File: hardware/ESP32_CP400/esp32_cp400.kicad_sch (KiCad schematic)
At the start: 20 parts, among them J2 USB_A, J3 USB_A, J4 USB_A, J5 Micro_SD_Card, J6 Barrel_Jack, J7 DA15_Pins

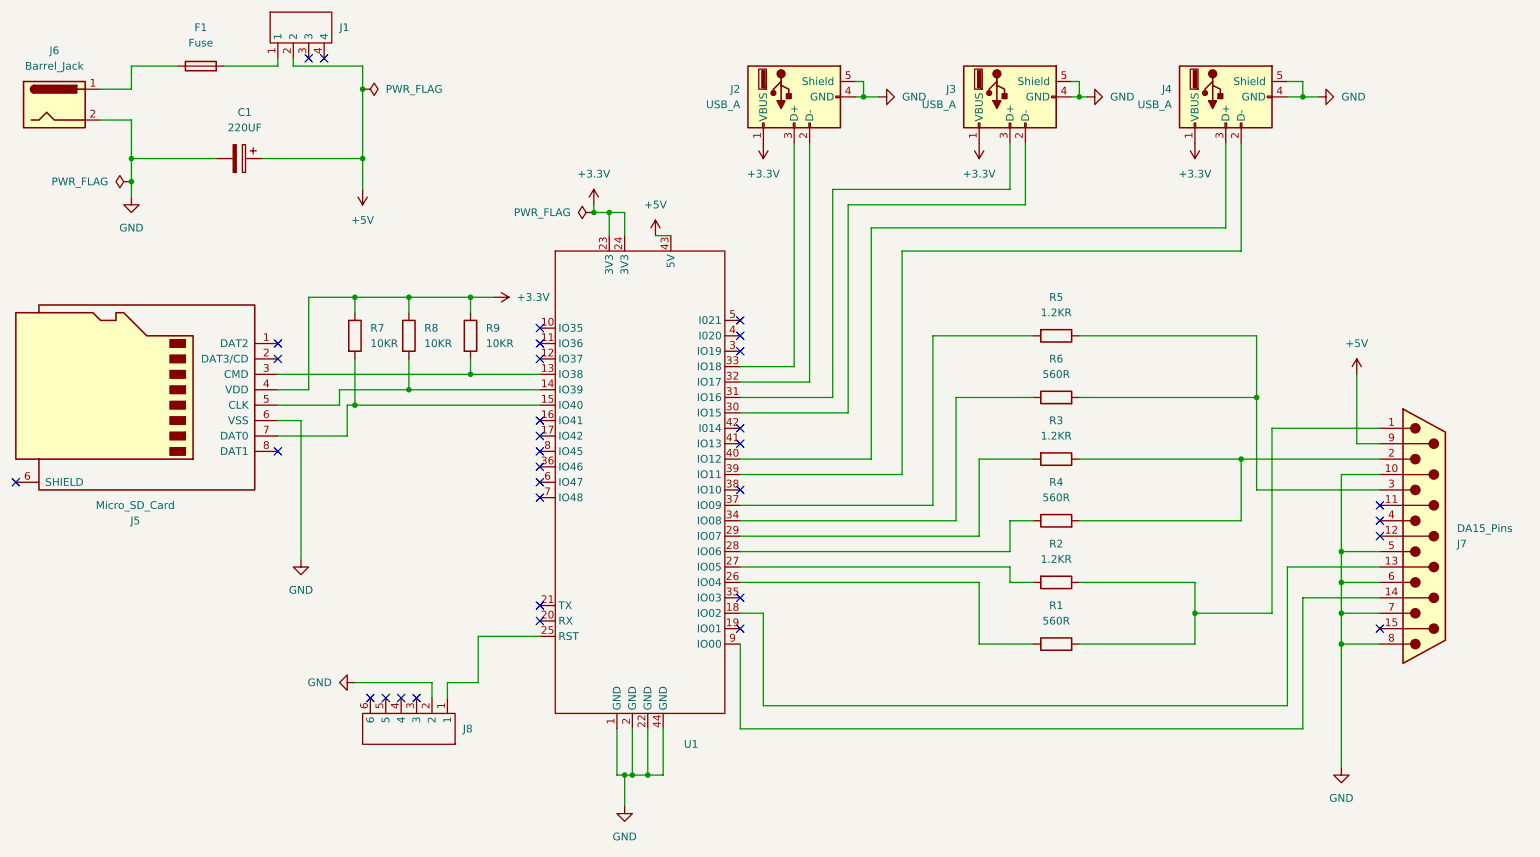
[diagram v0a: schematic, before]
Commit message: Add footprint for PJ-307 connector
- Created a new footprint file for the PJ-307 connector in the KiCad format.
- Included necessary attributes such as reference, value, and layer specifications.
- Defined pads for through-hole connections with appropriate sizes and drill specifications.
- Added graphical elements including lines and polygons for silk screen and fabrication layers.
- Provided a link to the datasheet for reference.
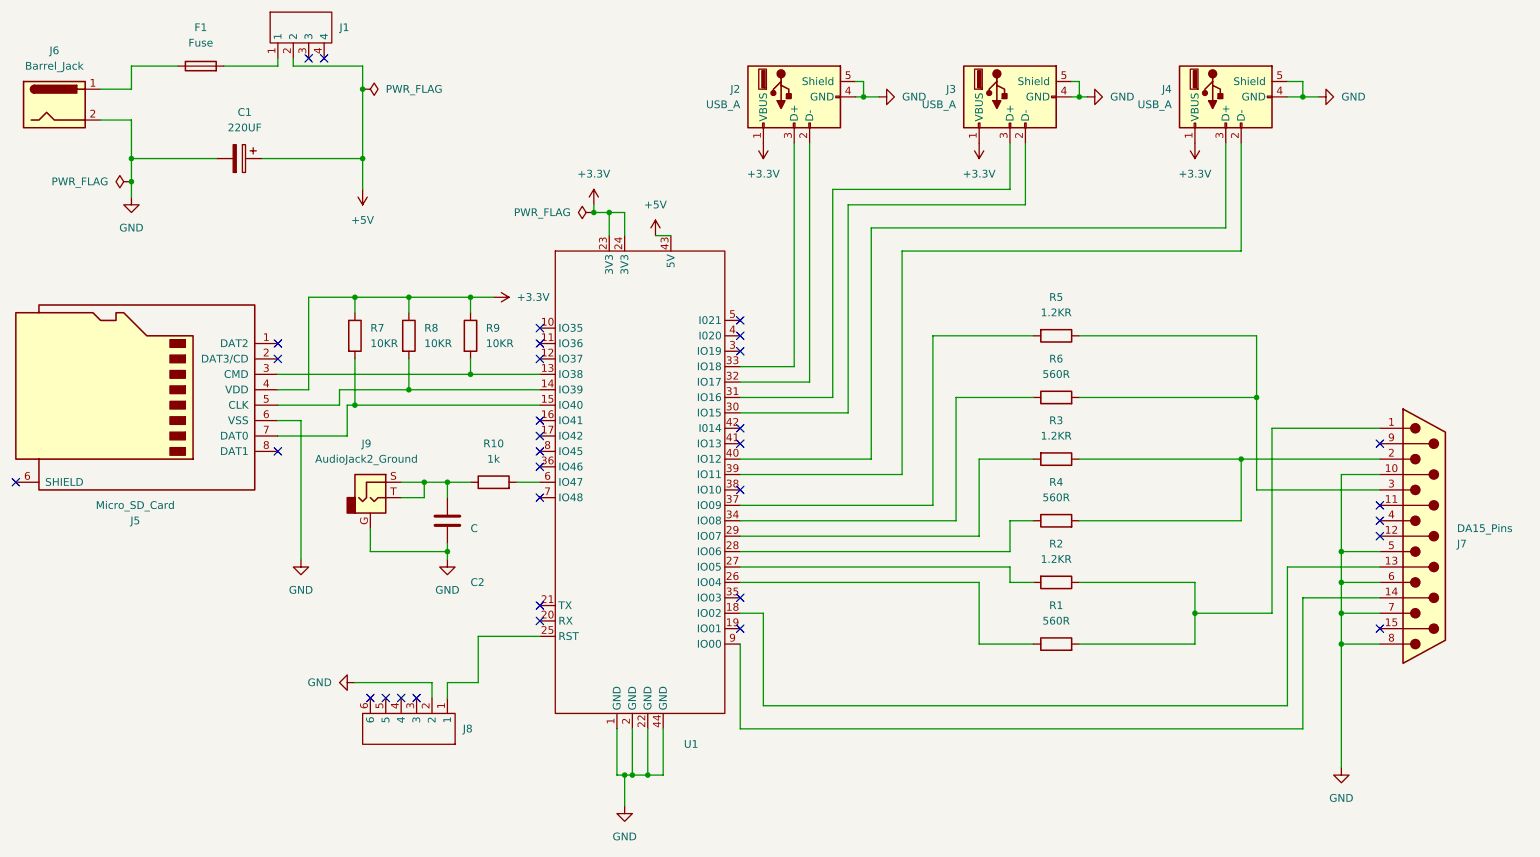
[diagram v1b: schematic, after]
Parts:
- added C2: C, Capacitor_SMD:C_0805_2012Metric_Pad1.18x1.45mm_HandSolder, symbol Device:C
- added J9: AudioJack2_Ground, PJ307:PJ-307, symbol Connector_Audio:AudioJack2_Ground
- added R10: 1k, Resistor_SMD:R_0805_2012Metric_Pad1.20x1.40mm_HandSolder, symbol Device:R
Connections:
- net +5V: no longer J7.9 (P9)
- net GND: now also C2.2, J9.G
- net at U1.6 (IO47): now also R10.2
- new net: C2.1, J9.S, J9.T, R10.1
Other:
- company: (none) -> The Retro Hacker
- title: (none) -> ESP32-CP400
